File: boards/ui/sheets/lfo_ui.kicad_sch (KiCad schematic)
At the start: 26 parts, among them Q1 2N3904, Q2 2N3904

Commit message: Added schematics docs
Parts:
- renumbered TP2 to TP25, TP2 to TP26
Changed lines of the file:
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@@
 		(dnp no)
 		(fields_autoplaced yes)
-		(property "Reference" "TP2"
+		(property "Reference" "TP25"
 			(at 81.28 127.508 0)
 			(effects
@@
 		(dnp no)
 		(fields_autoplaced yes)
-		(property "Reference" "TP2"
+		(property "Reference" "TP26"
 			(at 133.35 127.508 0)
 			(effects

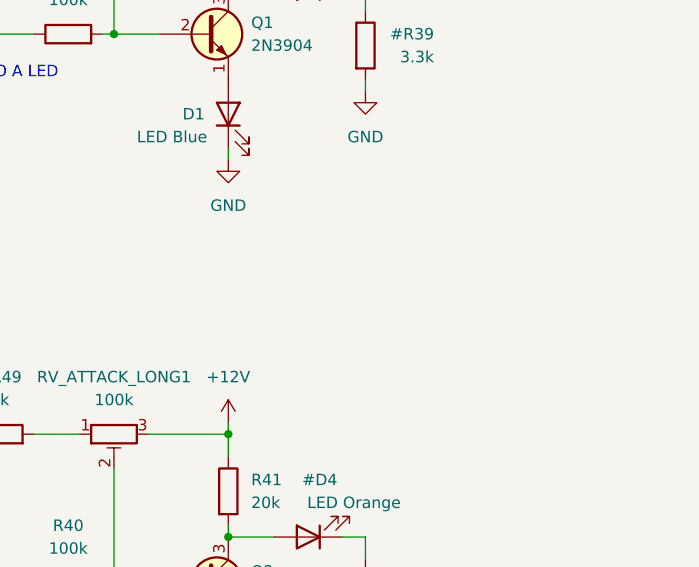
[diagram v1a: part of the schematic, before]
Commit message: Added LFO LED resistor values
https://github.com/shmoergh/hog/issues/24
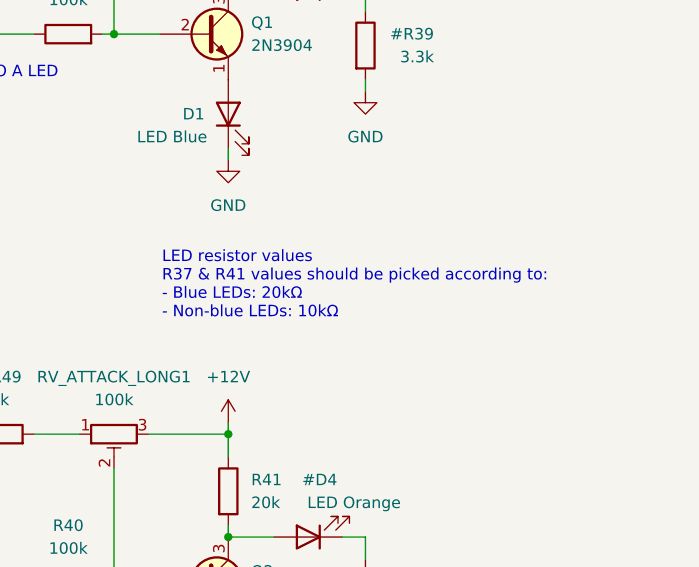
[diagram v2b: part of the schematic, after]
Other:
- note added: "LED resistor values R37 & R41 values should be picked according to: - Blue LEDs: 20kΩ - Non-blue LEDs: 10kΩ"
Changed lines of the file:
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@@
+		)
+	)
+	(text "LED resistor values\nR37 & R41 values should be picked according to:\n- Blue LEDs: 20kΩ\n- Non-blue LEDs: 10kΩ"
+		(exclude_from_sim no)
+		(at 222.504 99.06 0)
+		(effects
+			(font
+				(size 1.27 1.27)
+			)
+			(justify left bottom)
 		)
 	)

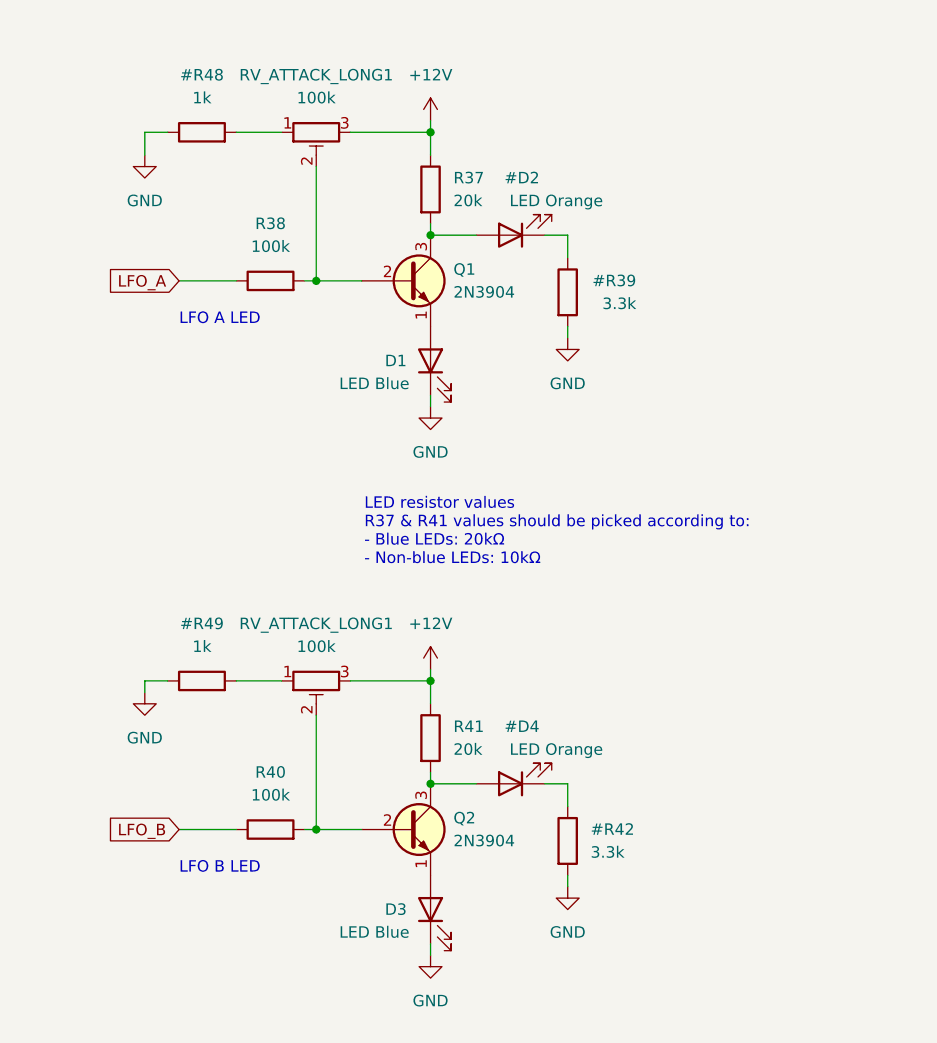
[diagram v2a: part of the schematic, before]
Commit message: Added production files for the UI board
ref https://github.com/shmoergh/hog/issues/19
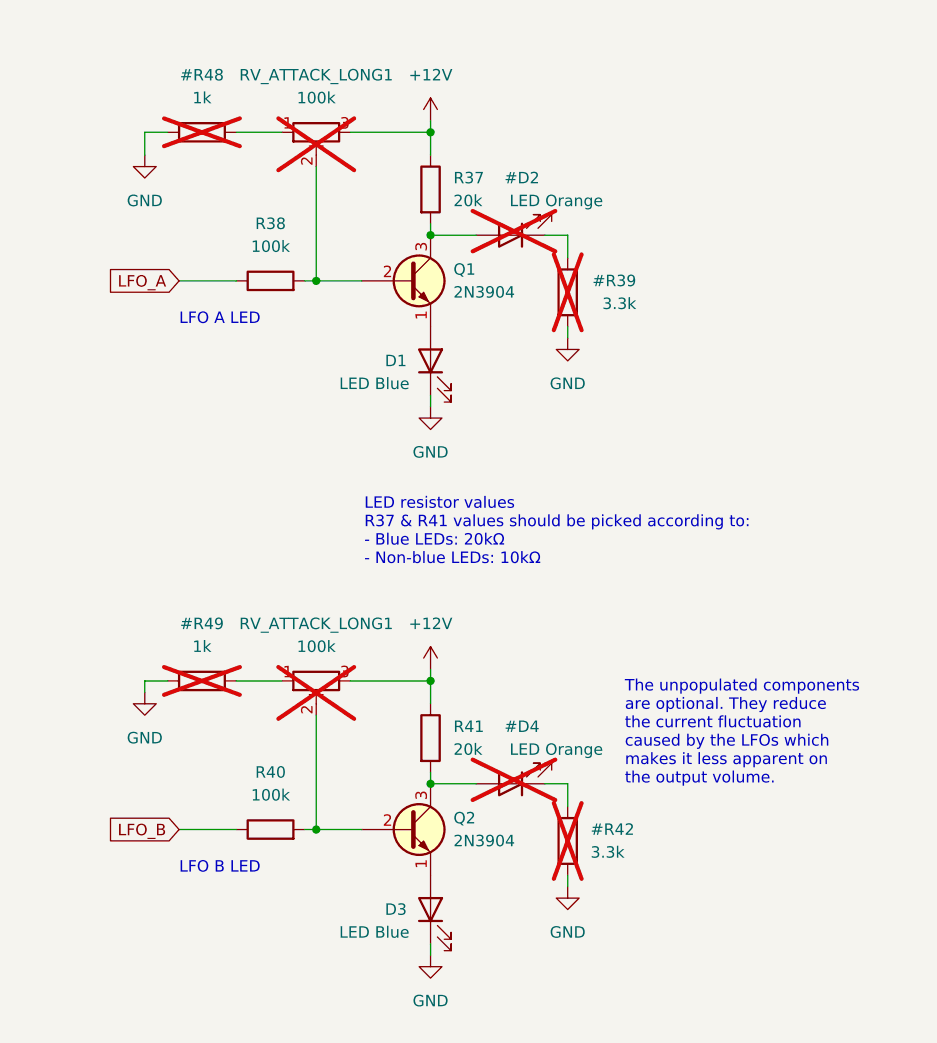
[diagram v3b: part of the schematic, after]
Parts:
- #D2, #D4, #R39, #R42, #R48, #R49: now not fitted; now left out of the parts list
- D1, D3: Part No. (none) -> 859-LTL-1CHG; Part URL (none) -> https://mou.sr/3OXMWKk; Vendor (none) -> Mouser
- Q1, Q2: Part No. (none) -> 637-2N3904; Part URL (none) -> https://mou.sr/4febysZ; Vendor (none) -> Mouser
- R37, R41: Part No. (none) -> 303-MF0W4FF1002T50; Part URL (none) -> https://mou.sr/3DjJ444; Vendor (none) -> Mouser
- R38, R40: Part No. (none) -> 303-MF0W4FF1003T50; Part URL (none) -> https://mou.sr/3BGpE8K; Vendor (none) -> Mouser
- R46, R47: Part No. (none) -> 303-MF0W4FF2200B00; Part URL (none) -> https://mou.sr/4iu83Sh; Vendor (none) -> Mouser
- RV_ATTACK_LONG1: Part No. (none) -> 652-3306F-1-104; Part URL (none) -> https://mou.sr/3OVBYFf; Vendor (none) -> Mouser; now not fitted; now left out of the parts list
- RV_LFO1_AMOUNT1, RV_LFO1_SPEED1, RV_LFO2_AMOUNT1, RV_LFO2_SPEED1: Part No. (none) -> 652-PTV09A-4025UA104; Part URL (none) -> https://mou.sr/44vDepN; Vendor (none) -> Mouser
- SW_VCO2_WAVE2, SW_VCO2_WAVE3: Part No. (none) -> TS23-E02; Part URL (none) -> https://www.aliexpress.com/item/32958319752.html?spm=a2g0o.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; Vendor (none) -> Daier
- TP25, TP26: now left out of the parts list
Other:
- note added: "The unpopulated components are optional. They reduce the current fluctuation caused by the LFOs which makes it less apparent on the output volume."

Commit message: Updated resistor Mouser no's and added full bom
- Some of the THT resistors in the BOM were referencing to products with min. 1000 pcs order quantity
- Added a full Mouser BOM which can be used to order all Mouser components by uploading to their BOM tool: https://hu.mouser.com/bom/
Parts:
- R37, R41: Part No. 303-MF0W4FF1002T50 -> 603-MFR-25FRF5220K; Part URL https://mou.sr/3DjJ444 -> https://mou.sr/4bBnUeQ
- R38, R40: Part No. 303-MF0W4FF1003T50 -> 603-MFR-25FRF52100K; Part URL https://mou.sr/3BGpE8K -> https://mou.sr/4hEwI4G
- R46, R47: Part No. 303-MF0W4FF2200B00 -> 603-MFR-25FTE52-220R; Part URL https://mou.sr/4iu83Sh -> https://mou.sr/428sz4x
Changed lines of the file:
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@@
 		(shape output)
 		(at 133.35 67.31 0)
-		(fields_autoplaced yes)
 		(effects
 			(font
@@
 		(shape output)
 		(at 161.29 88.9 0)
-		(fields_autoplaced yes)
 		(effects
 			(font
@@
 		(shape output)
 		(at 81.28 67.31 0)
-		(fields_autoplaced yes)
 		(effects
 			(font
@@
 			)
 		)
-		(property "Part No." "303-MF0W4FF1002T50 "
+		(property "Part No." "603-MFR-25FRF5220K"
 			(at 229.87 118.11 0)
 			(effects
@@
 			)
 		)
-		(property "Part URL" "https://mou.sr/3DjJ444"
+		(property "Part URL" "https://mou.sr/4bBnUeQ"
 			(at 229.87 118.11 0)
 			(effects
@@
 			)
 		)
-		(property "Part No." "303-MF0W4FF2200B00 "
+		(property "Part No." "603-MFR-25FTE52-220R"
 			(at 124.46 111.76 0)
 			(effects
@@
 			)
 		)
-		(property "Part URL" "https://mou.sr/4iu83Sh"
+		(property "Part URL" "https://mou.sr/428sz4x"
 			(at 124.46 111.76 0)
 			(effects
@@
 			)
 		)
-		(property "Part No." "303-MF0W4FF1003T50 "
+		(property "Part No." "603-MFR-25FRF52100K"
 			(at 212.09 67.31 0)
 			(effects
@@
 			)
 		)
-		(property "Part URL" "https://mou.sr/3BGpE8K"
+		(property "Part URL" "https://mou.sr/4hEwI4G"
 			(at 212.09 67.31 0)
 			(effects
@@
 			)
 		)
-		(property "Part No." "303-MF0W4FF1003T50 "
+		(property "Part No." "603-MFR-25FRF52100K"
 			(at 212.09 128.27 0)
 			(effects
@@
 			)
 		)
-		(property "Part URL" "https://mou.sr/3BGpE8K"
+		(property "Part URL" "https://mou.sr/4hEwI4G"
 			(at 212.09 128.27 0)
 			(effects
@@
 			)
 		)
-		(property "Part No." "303-MF0W4FF1002T50 "
+		(property "Part No." "603-MFR-25FRF5220K"
 			(at 229.87 57.15 0)
 			(effects
@@
 			)
 		)
-		(property "Part URL" "https://mou.sr/3DjJ444"
+		(property "Part URL" "https://mou.sr/4bBnUeQ"
 			(at 229.87 57.15 0)
 			(effects
@@
 			)
 		)
-		(property "Part No." "303-MF0W4FF2200B00 "
+		(property "Part No." "603-MFR-25FTE52-220R"
 			(at 72.39 111.76 0)
 			(effects
@@
 			)
 		)
-		(property "Part URL" "https://mou.sr/4iu83Sh"
+		(property "Part URL" "https://mou.sr/428sz4x"
 			(at 72.39 111.76 0)
 			(effects
